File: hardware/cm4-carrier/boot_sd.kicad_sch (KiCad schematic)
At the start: 25 parts, among them J8 microSD (CM4 Lite boot), Q2 DMG2305UX, Q3 2N7002, SW1 GLOBAL_EN, SW2 RUN_PG, SW3 nRPIBOOT

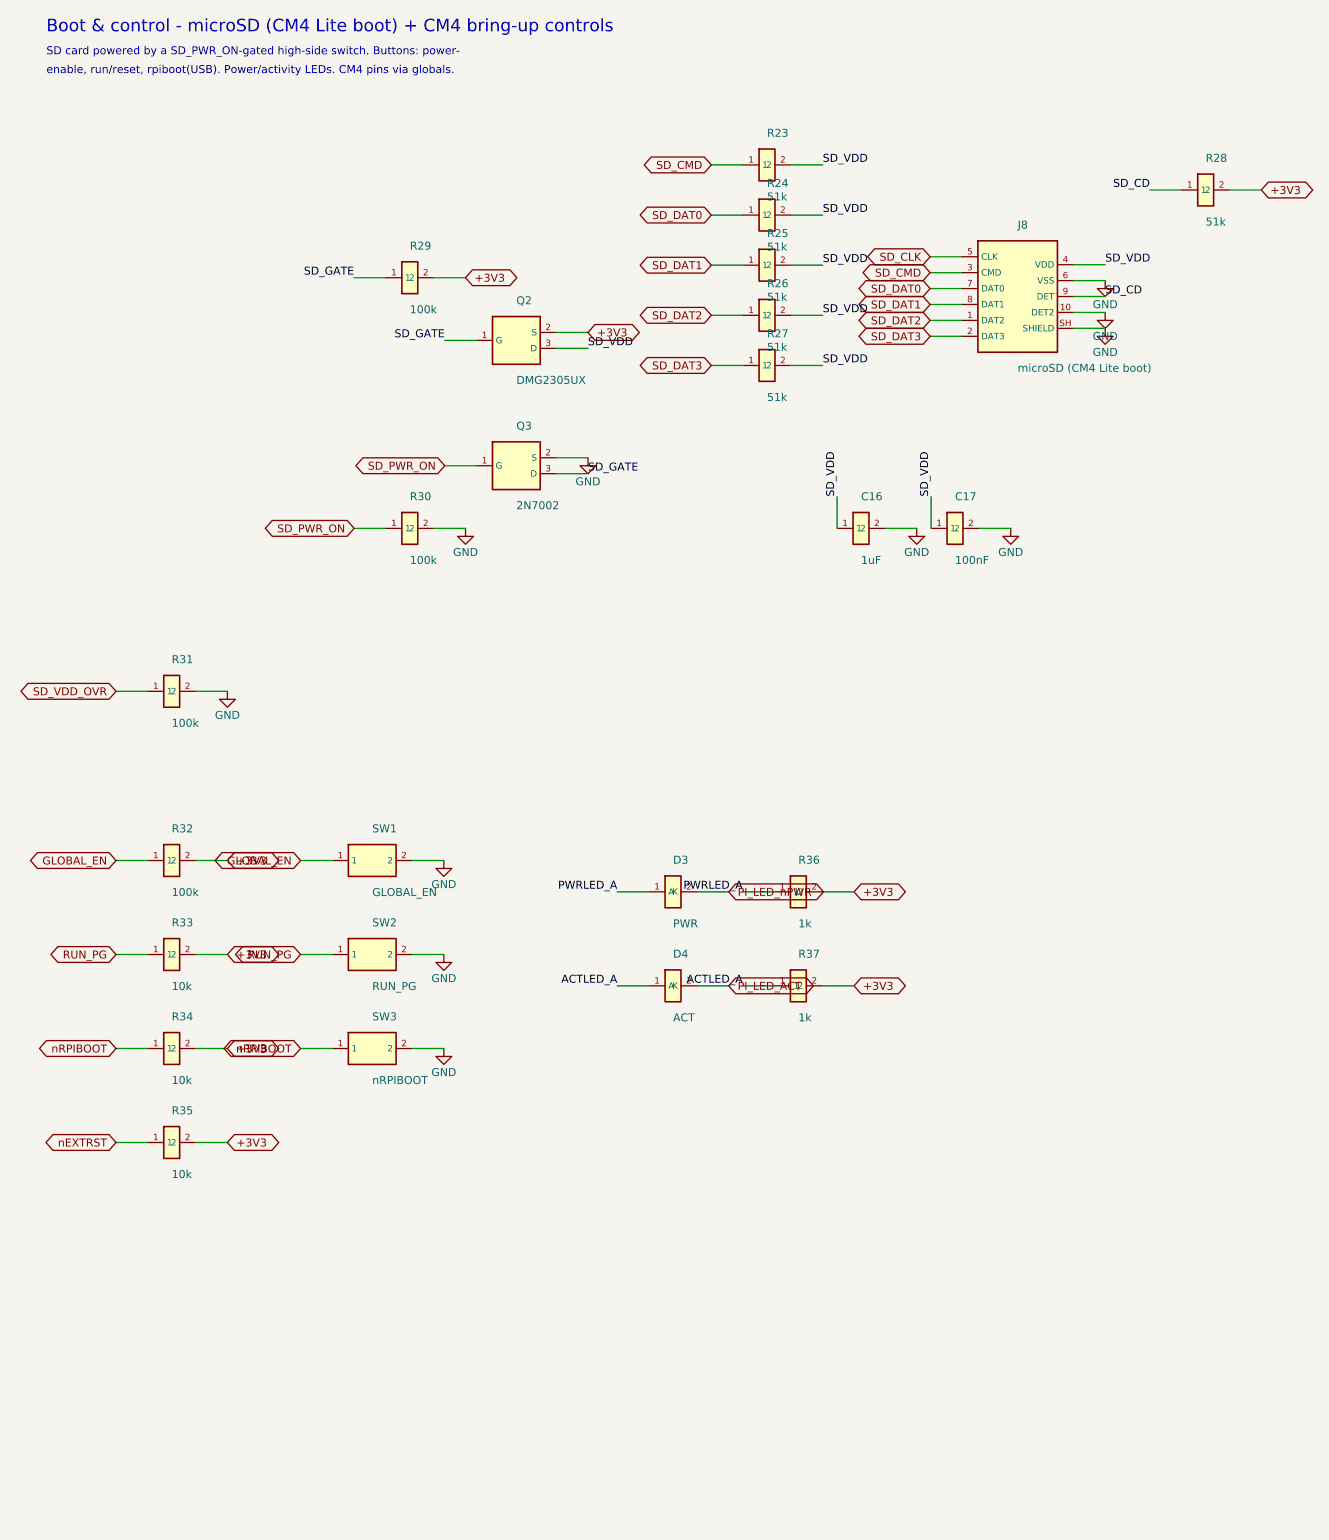
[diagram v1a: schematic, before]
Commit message: Add volume up/down and sleep/wake push buttons
Add three user push buttons on the boot/control sheet:

- SW4 (volume up, GPIO22) and SW5 (volume down, GPIO23): momentary to GND with
  a 10k pull-up to 3.3V and a 100nF RC-debounce cap each; software reads them
  to adjust playback level.
- SW6 (sleep/wake) on GPIO3: with dtoverlay=gpio-shutdown a press cleanly halts
  the CM4 to save battery, and GPIO3 (the wake-from-halt pin) wakes it again.
  GPIO3 is also I2C1 SCL (already pulled up by the fuel gauge), so no debounce
  cap is used.

The CM4 sheet now exports GPIO22/GPIO23 as global nets VOL_UP/VOL_DN; the
sleep button ties to the existing SCL/GPIO3 net. README/BOM updated. No format
change (KiCad 10 schematic 20260306).

Co-Authored-By: Claude Opus 4.8 <noreply@anthropic.com>
Claude-Session: https://claude.ai/code/session_015B7X7FE461jFSRaiTFdnFt
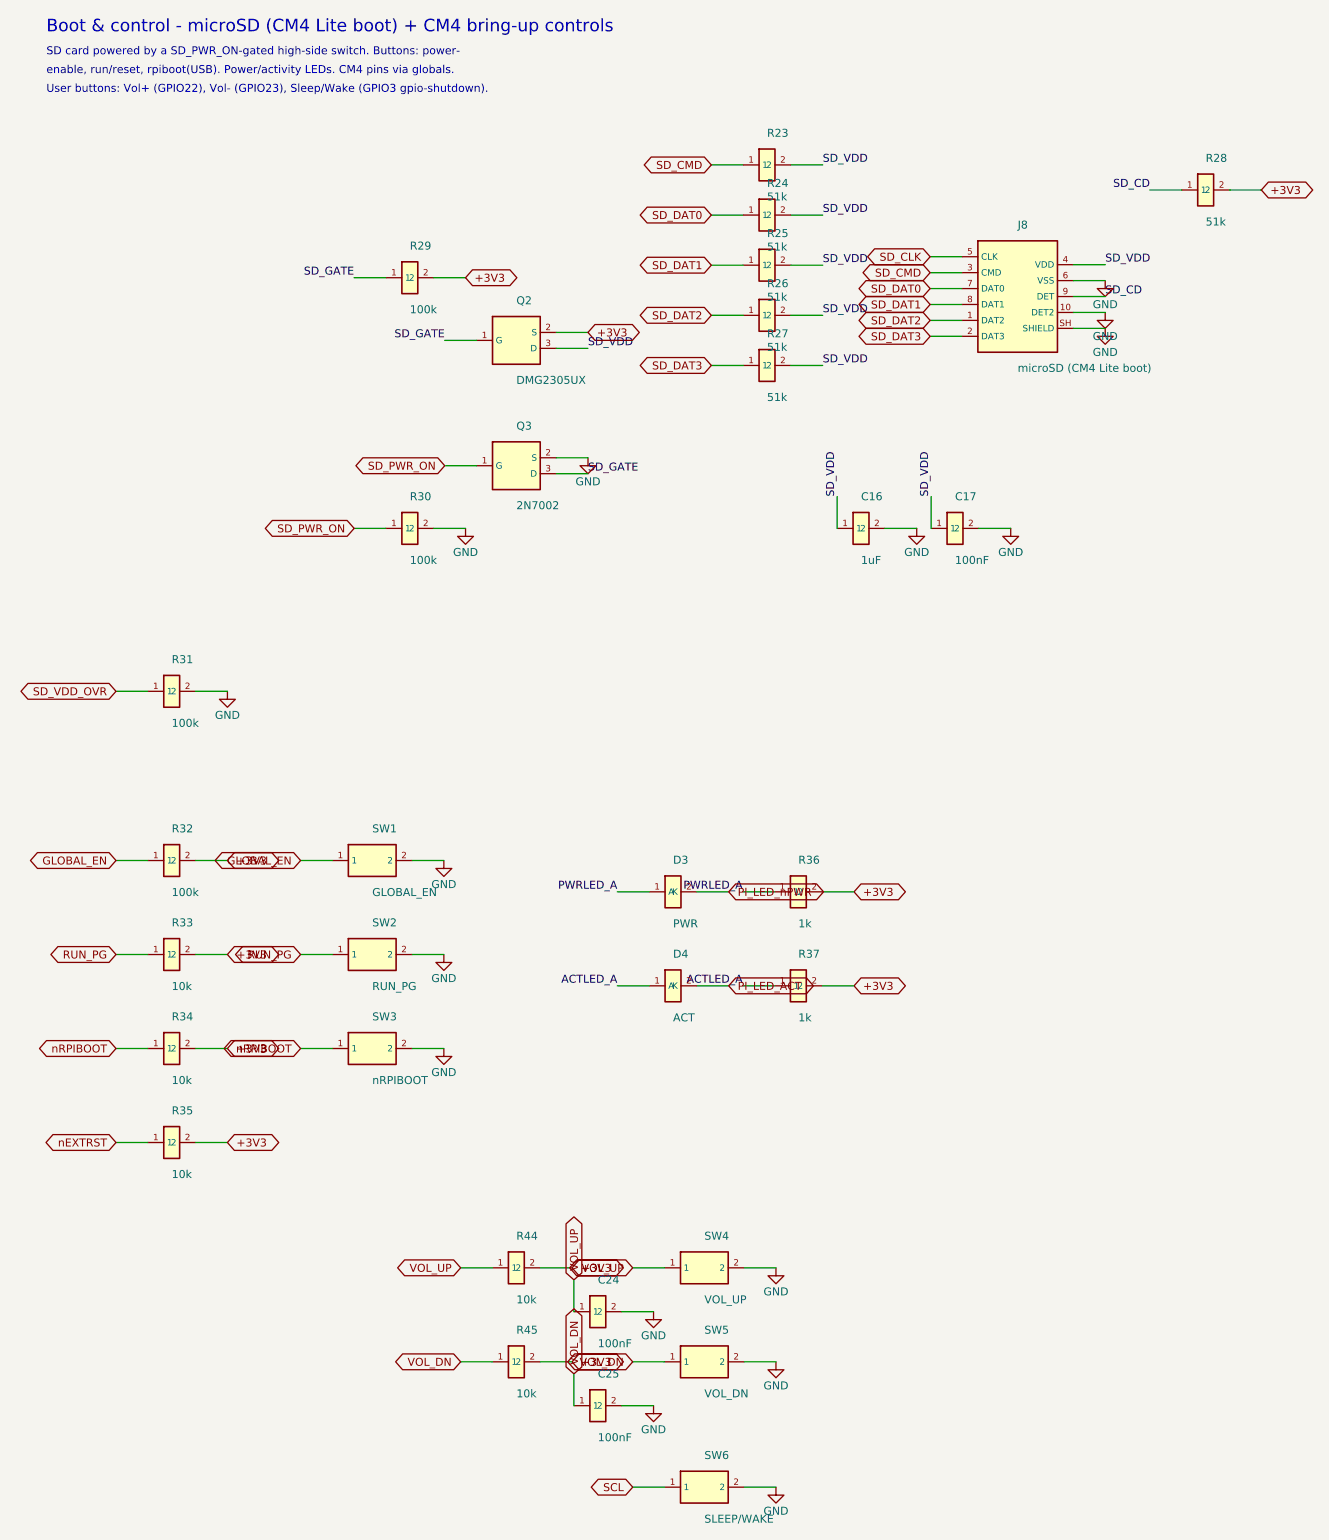
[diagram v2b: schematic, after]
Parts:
- added C24, C25: 100nF, Capacitor_SMD:C_0603_1608Metric, symbol carrier:C
- added R44, R45: 10k, Resistor_SMD:R_0402_1005Metric, symbol carrier:R
- added SW4: VOL_UP, Button_Switch_THT:SW_PUSH_6mm, symbol carrier:SW_Push
- added SW5: VOL_DN, Button_Switch_THT:SW_PUSH_6mm, symbol carrier:SW_Push
- added SW6: SLEEP/WAKE, Button_Switch_THT:SW_PUSH_6mm, symbol carrier:SW_Push
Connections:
- net +3V3: now also R44.2, R45.2
- net GND: now also C24.2, C25.2, SW4.2, SW5.2, SW6.2
- new net SCL: SW6.1
- new net VOL_DN: C25.1, R45.1, SW5.1
- new net VOL_UP: C24.1, R44.1, SW4.1
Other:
- note added: "User buttons: Vol+ (GPIO22), Vol- (GPIO23), Sleep/Wake (GPIO3 gpio-shutdown)."

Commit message: hardware: vertical FFC + side-angle buttons/LEDs, all with 3D models
Swap three component families to right-angle / edge-mount parts that are
Digi-Key-stocked and map to KiCad footprints that ship with 3D models:

- FFC J5/J6/J7: horizontal JUSHUO/Amphenol -> TE 1-84982-5, 15-pos 1.0 mm
  *vertical* SMT socket (Connector_FFC-FPC:TE_1-84982-5_2Rows-15Pins-P1.0mm_Vertical).
- Tact switches SW1-SW6: SW_PUSH_6mm -> C&K PTS645VL39-2 LFS, 6 mm
  side-actuated right-angle THT (Button_Switch_THT:SW_Tactile_SPST_Angled_PTS645Vx39-2LFS).
- LEDs D1-D4: 0603 -> Kingbright APA1606 side-view / right-angle
  (LED_SMD:LED_Kingbright_APA1606_1.6x0.6mm_Horizontal).

All replacement footprints keep pad names compatible with their symbols
(FFC 1-15, switch/LED 1-2), so Update PCB from Schematic stays clean.

Audited every footprint in the design: all resolve to KiCad library
footprints with a 3D model (only the MountingHole pads have no body, as
expected). README BOM, sourcing notes and bom-digikey.csv updated with the
new manufacturer part numbers.

Co-Authored-By: Claude Opus 4.8 <noreply@anthropic.com>
Claude-Session: https://claude.ai/code/session_019TySzotXwMtpz6QGTRfF9s
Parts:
- D3, D4: footprint LED_SMD:LED_0603_1608Metric -> LED_SMD:LED_Kingbright_APA1606_1.6x0.6mm_Horizontal
- SW1, SW2, SW3, SW4, SW5, SW6: footprint Button_Switch_THT:SW_PUSH_6mm -> Button_Switch_THT:SW_Tactile_SPST_Angled_PTS645Vx39-2LFS
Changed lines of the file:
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@@
 		(property "Value" "GLOBAL_EN" (at 72.00 150.08 0)
 			(effects (font (size 1.27 1.27)) (justify left)))
-		(property "Footprint" "Button_Switch_THT:SW_PUSH_6mm" (at 72.00 145.00 90)
+		(property "Footprint" "Button_Switch_THT:SW_Tactile_SPST_Angled_PTS645Vx39-2LFS" (at 72.00 145.00 90)
 			(effects (font (size 1.27 1.27)) (hide yes)))
 		(property "Datasheet" "" (at 72.00 145.00 0)
@@
 		(property "Value" "RUN_PG" (at 72.00 165.08 0)
 			(effects (font (size 1.27 1.27)) (justify left)))
-		(property "Footprint" "Button_Switch_THT:SW_PUSH_6mm" (at 72.00 160.00 90)
+		(property "Footprint" "Button_Switch_THT:SW_Tactile_SPST_Angled_PTS645Vx39-2LFS" (at 72.00 160.00 90)
 			(effects (font (size 1.27 1.27)) (hide yes)))
 		(property "Datasheet" "" (at 72.00 160.00 0)
@@
 		(property "Value" "nRPIBOOT" (at 72.00 180.08 0)
 			(effects (font (size 1.27 1.27)) (justify left)))
-		(property "Footprint" "Button_Switch_THT:SW_PUSH_6mm" (at 72.00 175.00 90)
+		(property "Footprint" "Button_Switch_THT:SW_Tactile_SPST_Angled_PTS645Vx39-2LFS" (at 72.00 175.00 90)
 			(effects (font (size 1.27 1.27)) (hide yes)))
 		(property "Datasheet" "" (at 72.00 175.00 0)
@@
 		(property "Value" "PWR" (at 120.00 155.08 0)
 			(effects (font (size 1.27 1.27)) (justify left)))
-		(property "Footprint" "LED_SMD:LED_0603_1608Metric" (at 120.00 150.00 90)
+		(property "Footprint" "LED_SMD:LED_Kingbright_APA1606_1.6x0.6mm_Horizontal" (at 120.00 150.00 90)
 			(effects (font (size 1.27 1.27)) (hide yes)))
 		(property "Datasheet" "" (at 120.00 150.00 0)
@@
 		(property "Value" "ACT" (at 120.00 170.08 0)
 			(effects (font (size 1.27 1.27)) (justify left)))
-		(property "Footprint" "LED_SMD:LED_0603_1608Metric" (at 120.00 165.00 90)
+		(property "Footprint" "LED_SMD:LED_Kingbright_APA1606_1.6x0.6mm_Horizontal" (at 120.00 165.00 90)
 			(effects (font (size 1.27 1.27)) (hide yes)))
 		(property "Datasheet" "" (at 120.00 165.00 0)
@@
 		(property "Value" "VOL_UP" (at 125.00 215.08 0)
 			(effects (font (size 1.27 1.27)) (justify left)))
-		(property "Footprint" "Button_Switch_THT:SW_PUSH_6mm" (at 125.00 210.00 90)
+		(property "Footprint" "Button_Switch_THT:SW_Tactile_SPST_Angled_PTS645Vx39-2LFS" (at 125.00 210.00 90)
 			(effects (font (size 1.27 1.27)) (hide yes)))
 		(property "Datasheet" "" (at 125.00 210.00 0)
@@
 		(property "Value" "VOL_DN" (at 125.00 230.08 0)
 			(effects (font (size 1.27 1.27)) (justify left)))
-		(property "Footprint" "Button_Switch_THT:SW_PUSH_6mm" (at 125.00 225.00 90)
+		(property "Footprint" "Button_Switch_THT:SW_Tactile_SPST_Angled_PTS645Vx39-2LFS" (at 125.00 225.00 90)
 			(effects (font (size 1.27 1.27)) (hide yes)))
 		(property "Datasheet" "" (at 125.00 225.00 0)
@@
 		(property "Value" "SLEEP/WAKE" (at 125.00 250.08 0)
 			(effects (font (size 1.27 1.27)) (justify left)))
-		(property "Footprint" "Button_Switch_THT:SW_PUSH_6mm" (at 125.00 245.00 90)
+		(property "Footprint" "Button_Switch_THT:SW_Tactile_SPST_Angled_PTS645Vx39-2LFS" (at 125.00 245.00 90)
 			(effects (font (size 1.27 1.27)) (hide yes)))
 		(property "Datasheet" "" (at 125.00 245.00 0)
